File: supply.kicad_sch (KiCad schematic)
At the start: 72 parts, among them J3 Molex_Nano-Fit_1x2_SMD_105430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, Q4 BCM857BS-7-F, Q5 BCM857BS-7-F

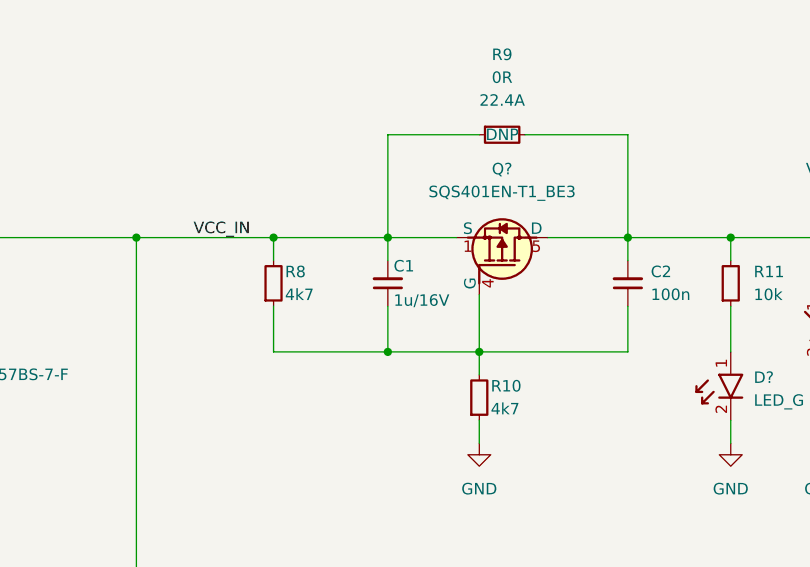
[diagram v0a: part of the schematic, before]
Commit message: [#54617] Reduce capacitors diversity
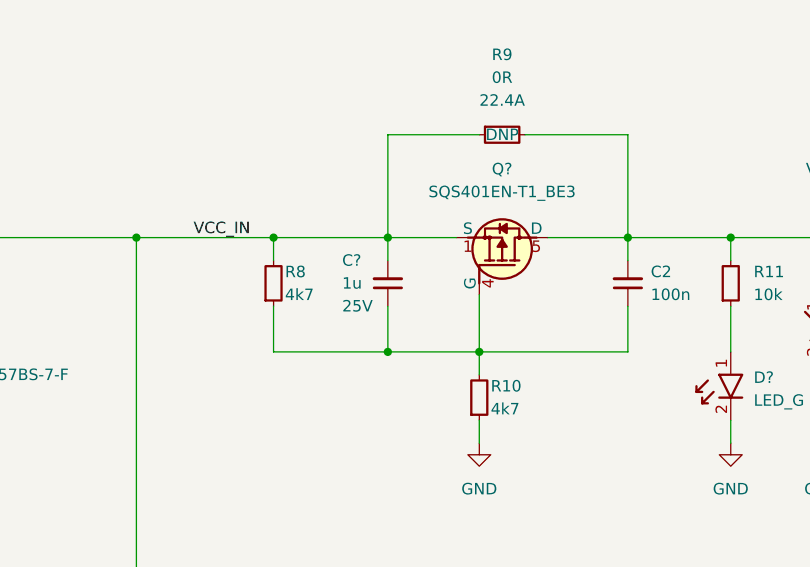
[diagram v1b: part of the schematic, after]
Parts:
- removed C1: C_1u_16V_0402, antmicro-footprints:C_0402_1005Metric, symbol antmicroCapacitors0402:C_1u_16V_0402
- added C?: C_1u_25V_0402, antmicro-footprints:C_0402_1005Metric, symbol antmicroCapacitors0402:C_1u_25V_0402
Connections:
- net VCC_IN: now also C?.2
- net at C2.1, Q?.4 (G), R10.2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: now also C?.1
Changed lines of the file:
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@@
     (pin "1")
   )
-  (symbol (lib_id "antmicroCapacitors0402:C_1u_16V_0402") (at 137.16 129.54 90) (unit 1)
+  (symbol (lib_id "antmicroCapacitors0402:C_1u_25V_0402") (at 137.16 129.54 90) (unit 1)
     (in_bom yes) (on_board yes)
-    (property "Reference" "C1" (id 0) (at 137.795 125.095 90)
+    (property "Reference" "C?" (id 0) (at 132.08 124.46 90)
+      (effects (font (size 1.27 1.27) (thickness 0.15)) (justify right))
+    )
+    (property "Value" "C_1u_25V_0402" (id 1) (at 147.32 109.22 0)
+      (effects (font (size 1.27 1.27) (thickness 0.15)) (justify left bottom) hide)
+    )
+    (property "Footprint" "antmicro-footprints:C_0402_1005Metric" (id 2) (at 149.86 109.22 0)
+      (effects (font (size 1.27 1.27) (thickness 0.15)) (justify left bottom) hide)
+    )
+    (property "Datasheet" "https://www.murata.com/products/productdetail?partno=GRM155R61E105KE11%23" (id 3) (at 152.4 109.22 0)
+      (effects (font (size 1.27 1.27) (thickness 0.15)) (justify left bottom) hide)
+    )
+    (property "MPN" "GRM155R61E105KE11J" (id 4) (at 154.94 109.22 0)
+      (effects (font (size 1.27 1.27) (thickness 0.15)) (justify left bottom) hide)
+    )
+    (property "Manufacturer" "Murata" (id 5) (at 157.48 109.22 0)
+      (effects (font (size 1.27 1.27) (thickness 0.15)) (justify left bottom) hide)
+    )
+    (property "License" "Apache-2.0" (id 6) (at 160.02 109.22 0)
+      (effects (font (size 1.27 1.27) (thickness 0.15)) (justify left bottom) hide)
+    )
+    (property "Author" "Antmicro" (id 7) (at 162.56 109.22 0)
+      (effects (font (size 1.27 1.27) (thickness 0.15)) (justify left bottom) hide)
+    )
+    (property "Val" "1u" (id 8) (at 132.08 127 90)
+      (effects (font (size 1.27 1.27) (thickness 0.15)) (justify right))
+    )
+    (property "Voltage" "25V" (id 9) (at 132.08 129.54 90)
       (effects (font (size 1.27 1.27)) (justify right))
     )
-    (property "Value" "C_1u_16V_0402" (id 1) (at 140.97 129.54 0)
-      (effects (font (size 1.524 1.524)) (justify left bottom) hide)
-    )
-    (property "Footprint" "antmicro-footprints:C_0402_1005Metric" (id 2) (at 132.08 124.46 0)
-      (effects (font (size 1.524 1.524)) (justify left bottom) hide)
-    )
-    (property "Datasheet" "https://www.kemet.com/en/us/capacitors/product/C0402C105M4PACTU.html" (id 3) (at 137.16 129.54 0)
+    (property "Dielectric" "X5R" (id 10) (at 167.64 109.22 0)
       (effects (font (size 1.27 1.27)) (justify left bottom) hide)
     )
-    (property "Manufacturer" "KEMET" (id 4) (at 127 124.46 0)
-      (effects (font (size 1.524 1.524)) (justify left bottom) hide)
-    )
-    (property "MPN" "C0402C105M4PACTU" (id 5) (at 129.54 124.46 0)
-      (effects (font (size 1.524 1.524)) (justify left bottom) hide)
-    )
-    (property "Val" "1u/16V" (id 6) (at 137.795 128.905 90)
-      (effects (font (size 1.27 1.27)) (justify right))
-    )
-    (property "License" "Apache-2.0" (id 7) (at 160.02 109.22 0)
-      (effects (font (size 1.27 1.27) (thickness 0.15)) (justify left bottom) hide)
-    )
-    (property "Author" "Antmicro" (id 8) (at 162.56 109.22 0)
-      (effects (font (size 1.27 1.27) (thickness 0.15)) (justify left bottom) hide)
-    )
-    (property "Voltage" "" (id 9) (at 165.1 109.22 0)
-      (effects (font (size 1.27 1.27)) (justify left bottom) hide)
-    )
-    (property "Dielectric" "" (id 10) (at 167.64 109.22 0)
-      (effects (font (size 1.27 1.27)) (justify left bottom) hide)
-    )

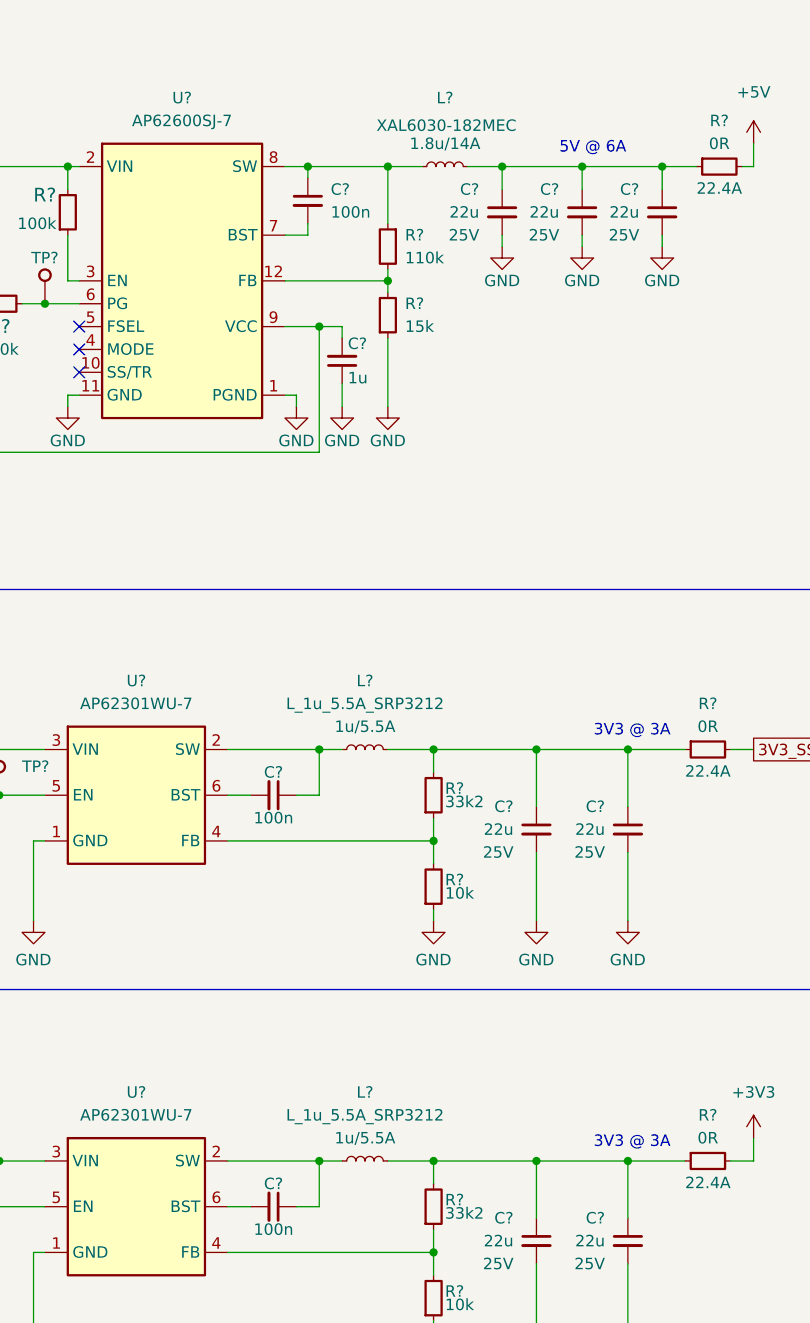
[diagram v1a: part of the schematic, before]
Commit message: [#54617] Migrate to KiCad 7
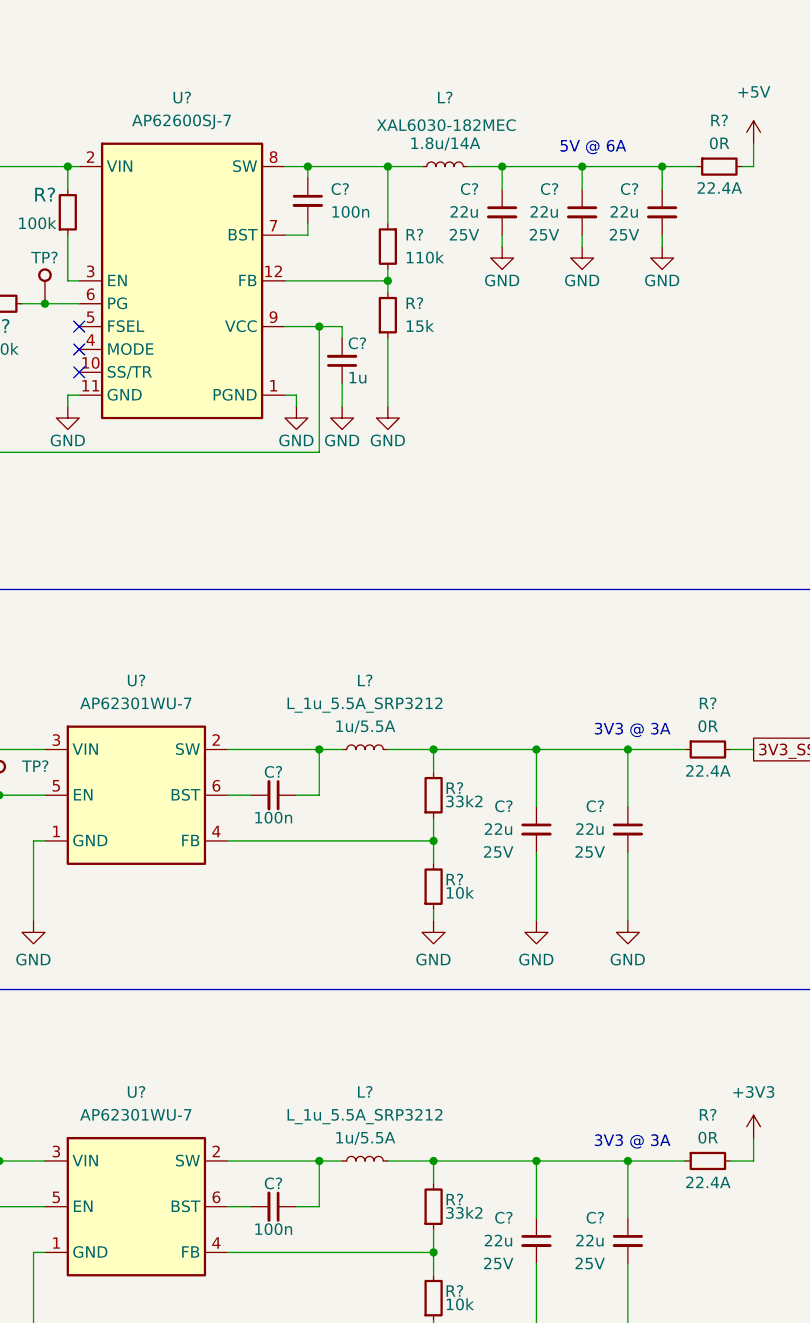
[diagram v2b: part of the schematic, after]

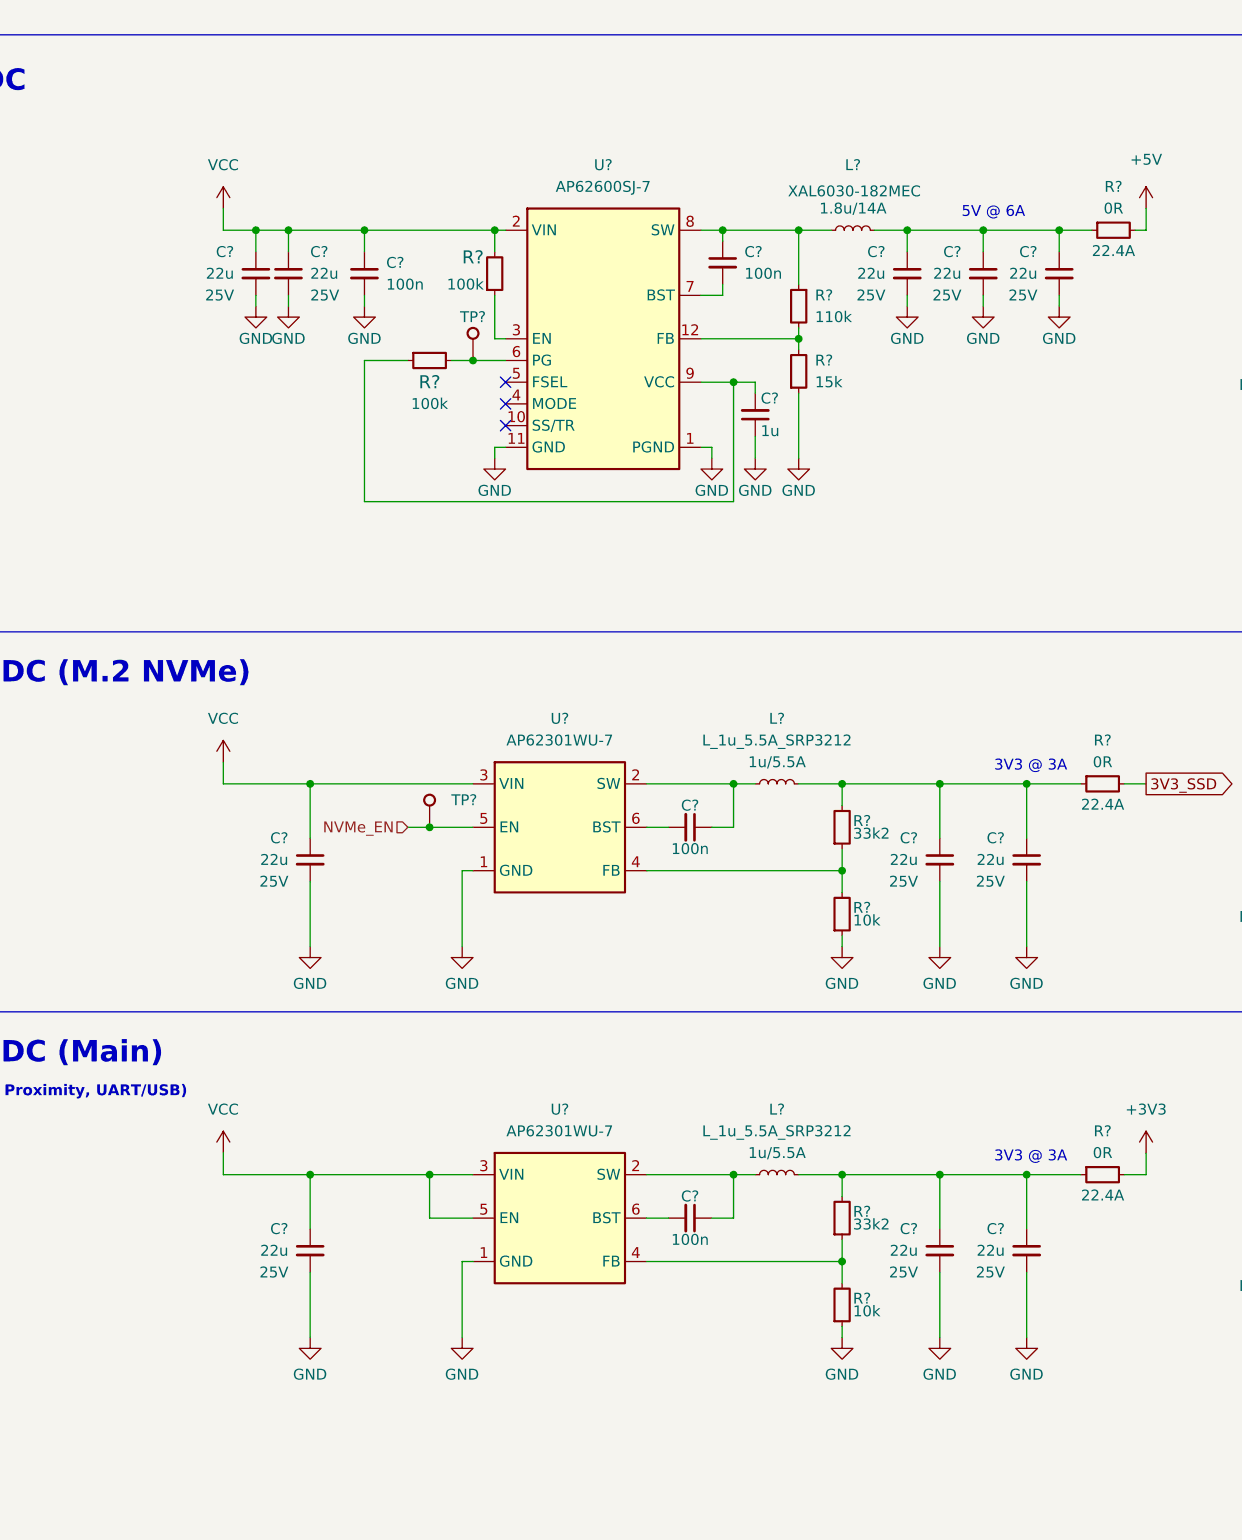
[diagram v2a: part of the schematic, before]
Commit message: [#54617] Review requested: change DCDC feedback resistors; add divider at EN
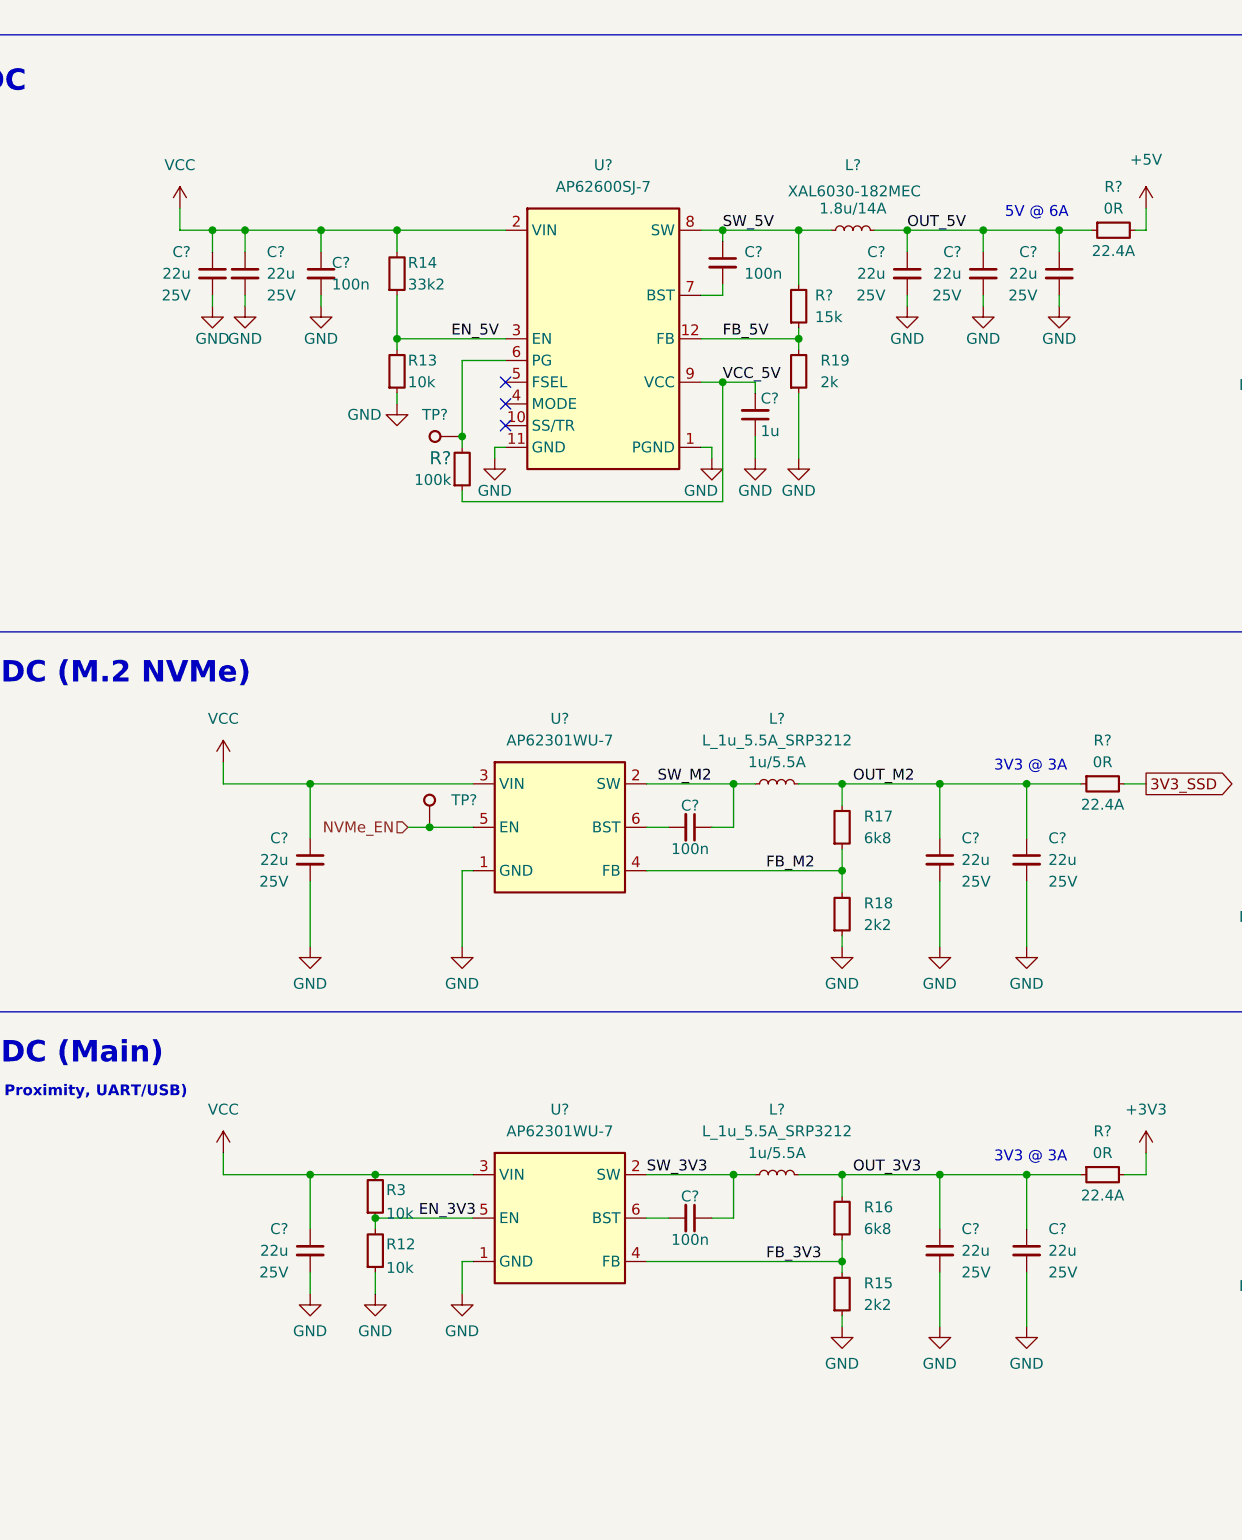
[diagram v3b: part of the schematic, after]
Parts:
- removed R? (x2): R_10k_0402, antmicro-footprints:R_0402_1005Metric, symbol antmicroResistors0402:R_10k_0402
- removed R? (x2): R_33k2_0402, antmicro-footprints:R_0402_1005Metric, symbol antmicroResistors0402:R_33k2_0402
- removed R?: R_110k_0402, antmicro-footprints:R_0402_1005Metric, symbol antmicroResistors0402:R_110k_0402
- removed R?: R_100k_0402, antmicro-footprints:R_0402_1005Metric, symbol antmicroResistors0402:R_100k_0402
- added R12, R13, R3: R_10k_0402, antmicro-footprints:R_0402_1005Metric, symbol antmicroResistors0402:R_10k_0402
- added R14: R_33k2_0402, antmicro-footprints:R_0402_1005Metric, symbol antmicroResistors0402:R_33k2_0402
- added R15, R18: R_2k2_0402, antmicro-footprints:R_0402_1005Metric, symbol antmicroResistors0402:R_2k2_0402
- added R16, R17: R_6k8_0402, antmicro-footprints:R_0402_1005Metric, symbol antmicroResistors0402:R_6k8_0402
- added R19: R_2k_0402, antmicro-footprints:R_0402_1005Metric, symbol antmicroResistors0402:R_2k_0402
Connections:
- net GND: now also R12.1, R13.1, R15.1, R18.1, R19.1; no longer R?.1
- net VCC: now also R14.2, R3.2; no longer U?.5 (EN)
- net OUT_5V: now reaches C?.1, C?.1, C?.1, L?.2, R?.1
- net SW_5V: now reaches C?.1, L?.1, U?.8 (SW)
- net SW_5V: now also R?.2
- net OUT_3V3: now reaches C?.1, C?.1, L?.2, R?.1
- net OUT_3V3: now also R16.2
- net VCC_5V: now reaches C?.2, R?.1, U?.9 (VCC)
- net SW_M2: now reaches C?.1, L?.1, U?.2 (SW)
- net OUT_M2: now reaches C?.1, C?.1, L?.2, R?.1
- net OUT_M2: now also R17.2
- net FB_M2: now reaches U?.4 (FB)
- net FB_M2: now also R17.1, R18.2
- net FB_5V: now reaches U?.12 (FB)
- net FB_5V: now also R?.1, R19.2; no longer R?.2
- net EN_5V: now reaches U?.3 (EN)
- net EN_5V: now also R13.2, R14.1
- net SW_3V3: now reaches C?.1, L?.1, U?.2 (SW)
- net FB_3V3: now reaches U?.4 (FB)
- net FB_3V3: now also R15.2, R16.1
- new net EN_3V3: R12.2, R3.1, U?.5 (EN)
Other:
- moved on the sheet: C?, R?, TP?
